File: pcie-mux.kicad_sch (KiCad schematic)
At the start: 51 parts, among them Q6 BSS138PW,115, Q7 BSS138PW,115, Q8 BSS138PW,115, SW1 SW_CVS-02B, U10 TMUXHS4412RUAR, U11 CBTL02043ABQ, U7 SY75602BTWL-TR, U8 74LVC1G157-Q100H_SOT457, U9 NTS0302JKZ

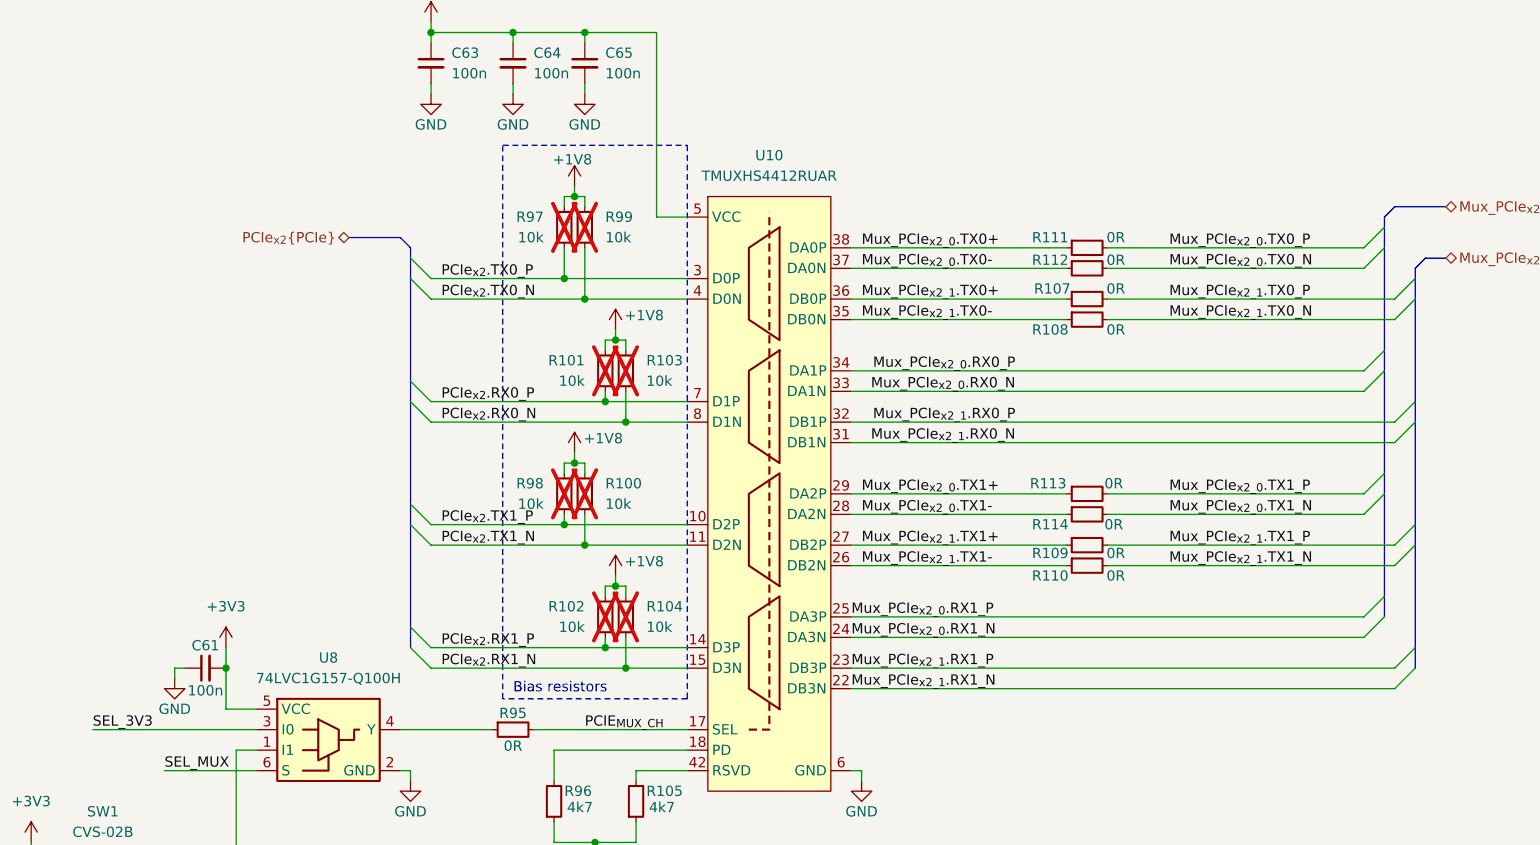
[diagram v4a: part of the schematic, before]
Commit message: [#101557] Add intentional PCIe polarity swap on U10
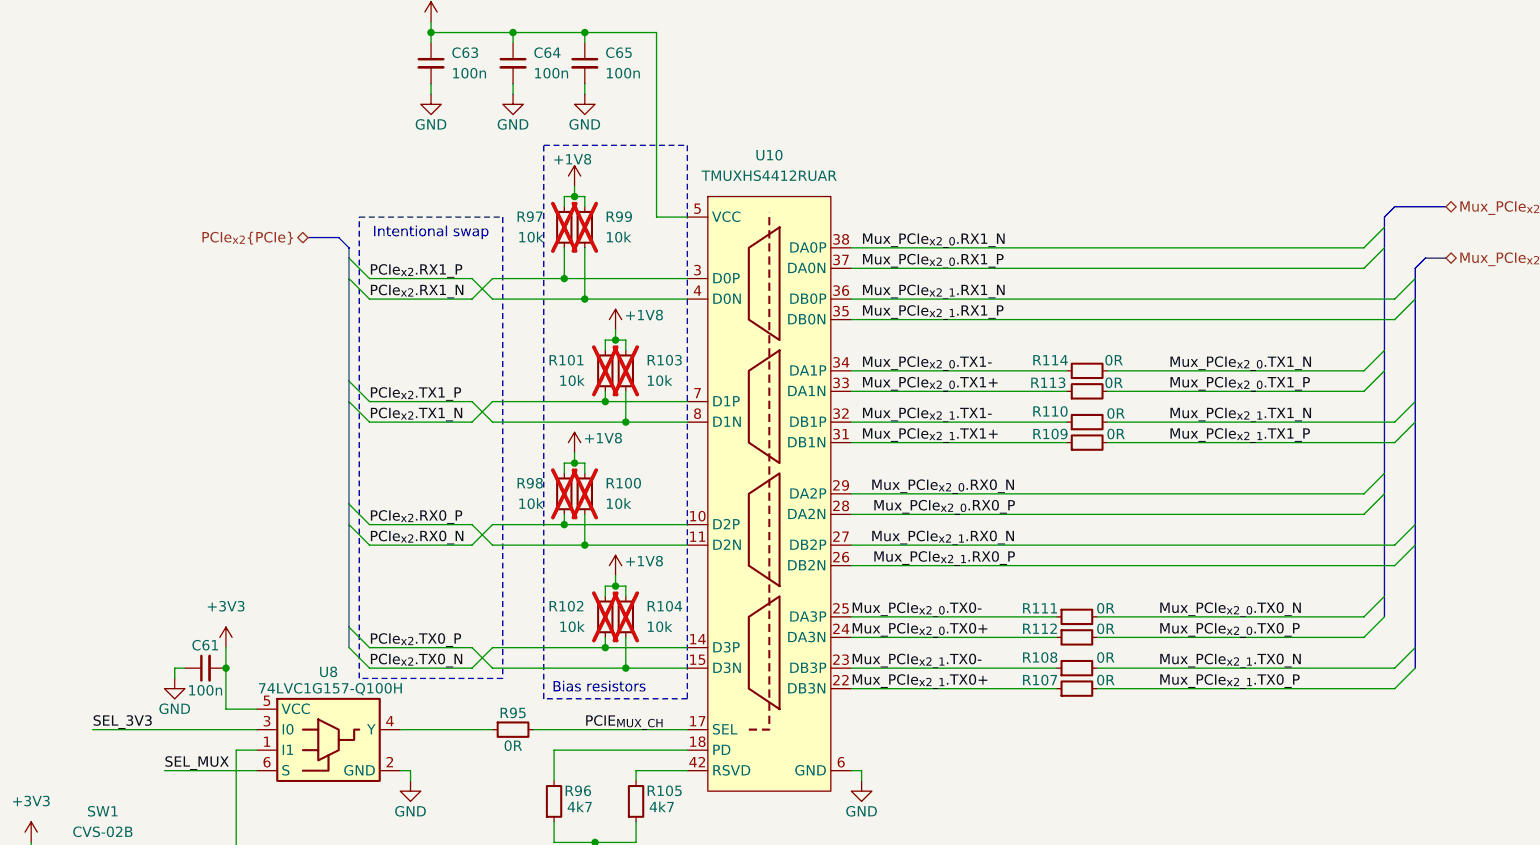
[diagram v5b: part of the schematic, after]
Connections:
- net Mux_PCIe_{x2_0}.RX0_N: now also U10.29 (DA2P); no longer U10.33 (DA1N)
- net Mux_PCIe_{x2_0}.RX0_P: now also U10.28 (DA2N); no longer U10.34 (DA1P)
- net Mux_PCIe_{x2_0}.RX1_N: now also U10.38 (DA0P); no longer U10.24 (DA3N)
- net Mux_PCIe_{x2_0}.RX1_P: now also U10.37 (DA0N); no longer U10.25 (DA3P)
- net Mux_PCIe_{x2_0}.TX0+: now also R112.1, U10.24 (DA3N); no longer R111.1, U10.38 (DA0P)
- net Mux_PCIe_{x2_0}.TX0-: now also R111.1, U10.25 (DA3P); no longer R112.1, U10.37 (DA0N)
- net Mux_PCIe_{x2_0}.TX0_N: now also R111.2; no longer R112.2
- net Mux_PCIe_{x2_0}.TX0_P: now also R112.2; no longer R111.2
- net Mux_PCIe_{x2_0}.TX1+: now also U10.33 (DA1N); no longer U10.29 (DA2P)
- net Mux_PCIe_{x2_0}.TX1-: now also U10.34 (DA1P); no longer U10.28 (DA2N)
- net Mux_PCIe_{x2_1}.RX0_N: now also U10.27 (DB2P); no longer U10.31 (DB1N)
- net Mux_PCIe_{x2_1}.RX0_P: now also U10.26 (DB2N); no longer U10.32 (DB1P)
- net Mux_PCIe_{x2_1}.RX1_N: now also U10.36 (DB0P); no longer U10.22 (DB3N)
- net Mux_PCIe_{x2_1}.RX1_P: now also U10.35 (DB0N); no longer U10.23 (DB3P)
- net Mux_PCIe_{x2_1}.TX0+: now also U10.22 (DB3N); no longer U10.36 (DB0P)
- net Mux_PCIe_{x2_1}.TX0-: now also U10.23 (DB3P); no longer U10.35 (DB0N)
- net Mux_PCIe_{x2_1}.TX1+: now also U10.31 (DB1N); no longer U10.27 (DB2P)
- net Mux_PCIe_{x2_1}.TX1-: now also U10.32 (DB1P); no longer U10.26 (DB2N)
- net PCIe_{x2}.RX0_N: now also R98.1, U10.10 (D2P); no longer R103.1, U10.8 (D1N)
- net PCIe_{x2}.RX0_P: now also R100.1, U10.11 (D2N); no longer R101.1, U10.7 (D1P)
- net PCIe_{x2}.RX1_N: now also R97.1, U10.3 (D0P); no longer R104.1, U10.15 (D3N)
- net PCIe_{x2}.RX1_P: now also R99.1, U10.4 (D0N); no longer R102.1, U10.14 (D3P)
- net PCIe_{x2}.TX0_N: now also R102.1, U10.14 (D3P); no longer R99.1, U10.4 (D0N)
- net PCIe_{x2}.TX0_P: now also R104.1, U10.15 (D3N); no longer R97.1, U10.3 (D0P)
- net PCIe_{x2}.TX1_N: now also R101.1, U10.7 (D1P); no longer R100.1, U10.11 (D2N)
- net PCIe_{x2}.TX1_P: now also R103.1, U10.8 (D1N); no longer R98.1, U10.10 (D2P)
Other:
- note added: "Intentional swap"
- moved on the sheet: R107, R108, R109, R110, R111, R112, R113, R114
